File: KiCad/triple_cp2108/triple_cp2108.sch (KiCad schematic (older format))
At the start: 29 parts, among them J1 USB_B, J2 USB_A, J27 Conn_02x20_Odd_Even, U1 MIC5504-3.3YM5, U2 USB2514B_Bi, Y1 24M

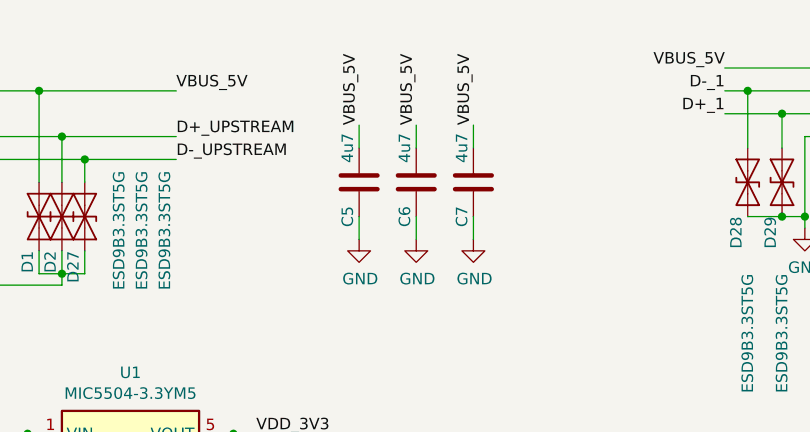
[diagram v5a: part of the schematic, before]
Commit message: BOM consolidation 1
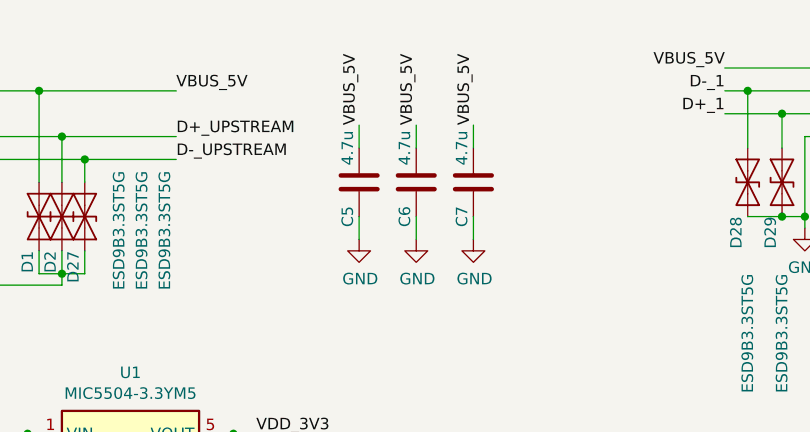
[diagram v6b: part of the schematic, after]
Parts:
- C5, C6, C7: value 4u7 -> 4.7u; footprint Capacitor_SMD:C_2225_5664Metric -> (none); Remark (none) -> X5R
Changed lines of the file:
@@
 P 2700 1200
 F 0 "C5" V 2750 1350 50  0000 C CNN
-F 1 "4u7" V 2750 1050 50  0000 C CNN
-F 2 "Capacitor_SMD:C_2225_5664Metric" H 2738 1050 50  0001 C CNN
+F 1 "4.7u" V 2750 1050 50  0000 C CNN
+F 2 "" H 2738 1050 50  0001 C CNN
 F 3 "~" H 2700 1200 50  0001 C CNN
+F 4 "X5R" H 2700 1200 50  0001 C CNN "Remark"
 	1    2700 1200
 	-1   0    0    1
@@
 P 2950 1200
 F 0 "C6" V 3000 1350 50  0000 C CNN
-F 1 "4u7" V 3000 1050 50  0000 C CNN
-F 2 "Capacitor_SMD:C_2225_5664Metric" H 2988 1050 50  0001 C CNN
+F 1 "4.7u" V 3000 1050 50  0000 C CNN
+F 2 "" H 2988 1050 50  0001 C CNN
 F 3 "~" H 2950 1200 50  0001 C CNN
+F 4 "X5R" H 2950 1200 50  0001 C CNN "Remark"
 	1    2950 1200
 	-1   0    0    1
@@
 P 3200 1200
 F 0 "C7" V 3250 1350 50  0000 C CNN
-F 1 "4u7" V 3250 1050 50  0000 C CNN
-F 2 "Capacitor_SMD:C_2225_5664Metric" H 3238 1050 50  0001 C CNN
+F 1 "4.7u" V 3250 1050 50  0000 C CNN
+F 2 "" H 3238 1050 50  0001 C CNN
 F 3 "~" H 3200 1200 50  0001 C CNN
+F 4 "X5R" H 3200 1200 50  0001 C CNN "Remark"
 	1    3200 1200
 	-1   0    0    1

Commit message: Netlist generated
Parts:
- C1, C2, C3, C4: footprint Capacitor_SMD:C_2225_5664Metric -> Capacitor_SMD:C_0805_2012Metric_Pad1.18x1.45mm_HandSolder
- C5, C6, C7: footprint (none) -> Capacitor_SMD:C_0805_2012Metric_Pad1.18x1.45mm_HandSolder
- J3: renamed from J27; footprint (none) -> Connector_PinHeader_2.54mm:PinHeader_2x20_P2.54mm_Vertical
- R1, R2, R3, R4: footprint Resistor_SMD:R_1206_3216Metric -> Resistor_SMD:R_0805_2012Metric_Pad1.20x1.40mm_HandSolder
- Y1: footprint (none) -> Crystal:Crystal_SMD_2016-4Pin_2.0x1.6mm; Manufacturer_Part_Number (none) -> XRCGB24M000F2P02R0; Mouser Price/Stock (none) -> https://www.eleparts.co.kr/goods/view?no=7918955
- renumbered D34 to D10, D35 to D11, D36 to D12, D27 to D3, D28 to D4, D29 to D5, D30 to D6, D31 to D7, D32 to D8, D33 to D9

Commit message: Netlist #2
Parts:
- C1, C2: value 18p -> 6p
- Y1: Manufacturer_Part_Number XRCGB24M000F2P02R0 -> XRCGB24M000F2P00R0
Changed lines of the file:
@@
 Text Label 3950 5850 0    50   ~ 0
 D+_4
-$Comp
-L Device:Crystal_Small Y1
-U 1 1 5FE8EB29
-P 1200 5450
-F 0 "Y1" H 1300 5350 50  0000 C CNN
-F 1 "24M" H 1100 5350 50  0000 C CNN
-F 2 "Crystal:Crystal_SMD_2016-4Pin_2.0x1.6mm" H 1200 5450 50  0001 C CNN
-F 3 "~" H 1200 5450 50  0001 C CNN
-F 4 "XRCGB24M000F2P02R0" H 1200 5450 50  0001 C CNN "Manufacturer_Part_Number"
-F 5 "https://www.eleparts.co.kr/goods/view?no=7918955" H 1200 5450 50  0001 C CNN "Mouser Price/Stock"
-	1    1200 5450
-	0    1    1    0
-$EndComp
-Wire Wire Line
-	1400 5250 1400 5300
-Wire Wire Line
-	1500 5650 1400 5650
-Wire Wire Line
-	1400 5650 1400 5600
-$Comp
-L Device:R R1
-U 1 1 5FE92ED4
-P 1400 5450
-F 0 "R1" V 1300 5300 50  0000 L CNN
-F 1 "1M" V 1300 5500 50  0000 L CNN
-F 2 "Resistor_SMD:R_0805_2012Metric_Pad1.20x1.40mm_HandSolder" V 1330 5450 50  0001 C CNN
-F 3 "~" H 1400 5450 50  0001 C CNN
-	1    1400 5450
-	1    0    0    -1
-$EndComp
-Wire Wire Line
-	1200 5350 1200 5250
-Wire Wire Line
-	1200 5250 1400 5250
-Connection ~ 1400 5250
-Wire Wire Line
-	1400 5650 1200 5650
-Wire Wire Line
-	1200 5650 1200 5550
-Connection ~ 1400 5650
-$Comp
-L Device:C C1
-U 1 1 5FE9A7F7
-P 900 5250
-F 0 "C1" V 800 5150 50  0000 C CNN
-F 1 "18p" V 800 5400 50  0000 C CNN
-F 2 "Capacitor_SMD:C_0805_2012Metric_Pad1.18x1.45mm_HandSolder" H 938 5100 50  0001 C CNN
-F 3 "~" H 900 5250 50  0001 C CNN
-	1    900  5250
-	0    1    1    0
-$EndComp
-$Comp
-L Device:C C2
-U 1 1 5FE9B6E0
-P 900 5650
-F 0 "C2" V 1000 5550 50  0000 C CNN
-F 1 "18p" V 1000 5800 50  0000 C CNN
-F 2 "Capacitor_SMD:C_0805_2012Metric_Pad1.18x1.45mm_HandSolder" H 938 5500 50  0001 C CNN
-F 3 "~" H 900 5650 50  0001 C CNN
-	1    900  5650
-	0    1    1    0
-$EndComp
-Wire Wire Line
-	1050 5650 1200 5650
-Connection ~ 1200 5650
-Wire Wire Line
-	1200 5250 1050 5250
-Connection ~ 1200 5250
 Wire Wire Line
 	750  5250 650  5250
 Wire Wire Line
 	650  5250 650  5300
-Wire Wire Line
-	750  5650 650  5650
-Wire Wire Line
-	650  5650 650  5700
 $Comp
 L power:GND #PWR01
@@
 	1    0    0    -1
 $EndComp
-$Comp
-L power:GND #PWR02
-U 1 1 5FEA2CD9
-P 650 5700
-F 0 "#PWR02" H 650 5450 50  0001 C CNN
-F 1 "GND" H 655 5527 50  0000 C CNN
-F 2 "" H 650 5700 50  0001 C CNN
-F 3 "" H 650 5700 50  0001 C CNN
-	1    650  5700
-	1    0    0    -1
-$EndComp
-Wire Wire Line
-	1400 5250 1600 5250
-Wire Wire Line
-	1600 5350 1500 5350
-Wire Wire Line
-	1500 5350 1500 5650
 Wire Wire Line
 	1600 5050 1450 5050
@@
 F13 "GPIO15" B R 9800 1400 50
 $EndSheet
+Wire Wire Line
+	1400 5250 1600 5250
+Connection ~ 1400 5250
+Wire Wire Line
+	1400 5250 1400 5300
+Wire Wire Line
+	1200 5250 1050 5250
+Wire Wire Line
+	1200 5250 1400 5250
+Connection ~ 1200 5250
+Wire Wire Line
+	1200 5350 1200 5250
+Wire Wire Line
+	1600 5350 1500 5350
+Wire Wire Line
+	1500 5350 1500 5650
+Wire Wire Line
+	650  5650 650  5700
+Wire Wire Line
+	750  5650 650  5650
+Wire Wire Line
+	1050 5650 1200 5650
+Wire Wire Line
+	1200 5650 1200 5550
+Connection ~ 1200 5650
+Wire Wire Line
+	1400 5650 1200 5650
+Wire Wire Line
+	1400 5650 1400 5600
+Connection ~ 1400 5650
+Wire Wire Line
+	1500 5650 1400 5650
+$Comp
+L power:GND #PWR02
+U 1 1 5FEA2CD9
+P 650 5700
+F 0 "#PWR02" H 650 5450 50  0001 C CNN
+F 1 "GND" H 655 5527 50  0000 C CNN
+F 2 "" H 650 5700 50  0001 C CNN
+F 3 "" H 650 5700 50  0001 C CNN
+	1    650  5700
+	1    0    0    -1
+$EndComp
+$Comp
+L Device:C C2
+U 1 1 5FE9B6E0
+P 900 5650
+F 0 "C2" V 1000 5550 50  0000 C CNN
+F 1 "6p" V 1000 5800 50  0000 C CNN
+F 2 "Capacitor_SMD:C_0805_2012Metric_Pad1.18x1.45mm_HandSolder" H 938 5500 50  0001 C CNN
+F 3 "~" H 900 5650 50  0001 C CNN
+	1    900  5650
+	0    1    1    0
+$EndComp
+$Comp
+L Device:C C1
+U 1 1 5FE9A7F7
+P 900 5250
+F 0 "C1" V 800 5150 50  0000 C CNN
+F 1 "6p" V 800 5400 50  0000 C CNN
+F 2 "Capacitor_SMD:C_0805_2012Metric_Pad1.18x1.45mm_HandSolder" H 938 5100 50  0001 C CNN
+F 3 "~" H 900 5250 50  0001 C CNN
+	1    900  5250
+	0    1    1    0
+$EndComp
+$Comp
+L Device:Crystal_Small Y1
+U 1 1 5FE8EB29
+P 1200 5450
+F 0 "Y1" H 1300 5350 50  0000 C CNN
+F 1 "24M" H 1100 5350 50  0000 C CNN
+F 2 "Crystal:Crystal_SMD_2016-4Pin_2.0x1.6mm" H 1200 5450 50  0001 C CNN
+F 3 "~" H 1200 5450 50  0001 C CNN
+F 4 "XRCGB24M000F2P00R0" H 1200 5450 50  0001 C CNN "Manufacturer_Part_Number"
+F 5 "https://www.eleparts.co.kr/goods/view?no=7918955" H 1200 5450 50  0001 C CNN "Mouser Price/Stock"
+	1    1200 5450
+	0    1    1    0
+$EndComp
+$Comp
+L Device:R R1
+U 1 1 5FE92ED4
+P 1400 5450
+F 0 "R1" V 1300 5300 50  0000 L CNN
+F 1 "1M" V 1300 5500 50  0000 L CNN
+F 2 "Resistor_SMD:R_0805_2012Metric_Pad1.20x1.40mm_HandSolder" V 1330 5450 50  0001 C CNN
+F 3 "~" H 1400 5450 50  0001 C CNN
+	1    1400 5450
+	1    0    0    -1
+$EndComp
 $EndSCHEMATC
